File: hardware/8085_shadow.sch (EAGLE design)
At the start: 56 parts, among them IC11 74HCT245DW, IC2 74HCT574N, IC3 74LVC1G04DBV, IC5 74HCT245DW, IC6 74AC273N, IC7 74LVC1G79DBV, IC9 74HCT138N

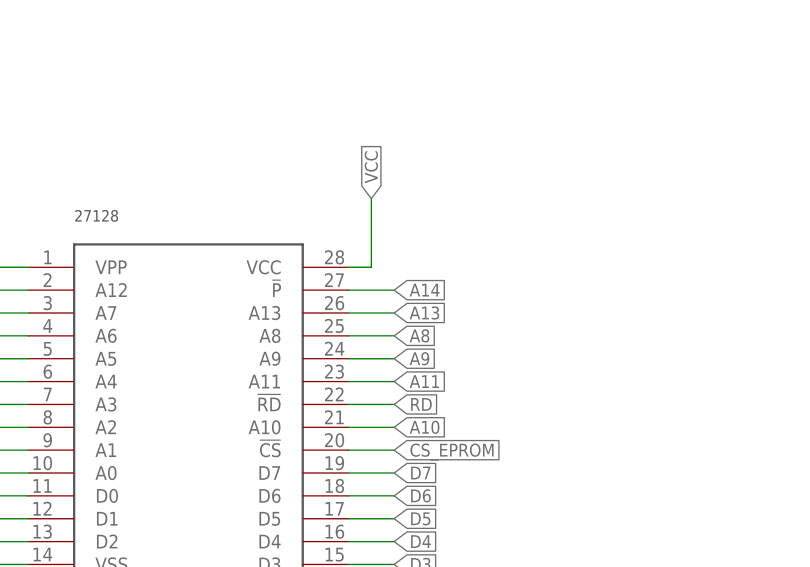
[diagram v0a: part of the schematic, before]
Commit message: Bug in PCB design fixed
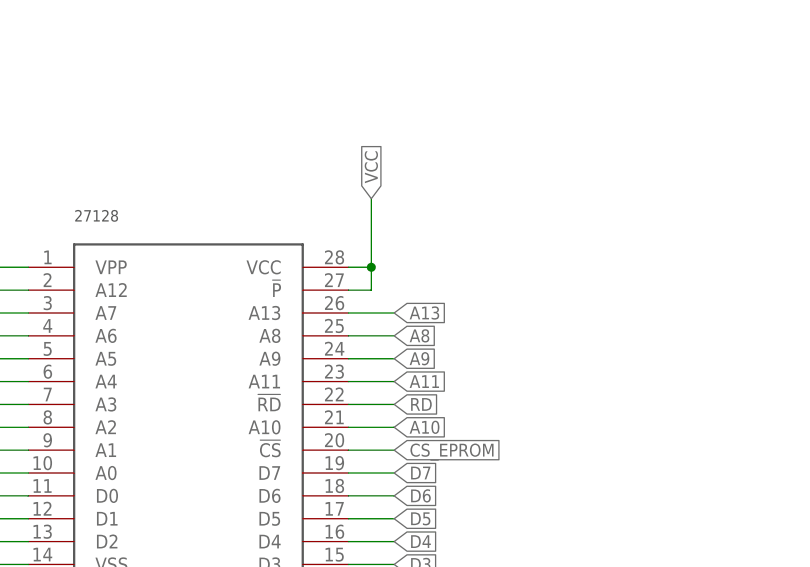
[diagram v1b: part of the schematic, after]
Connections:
- net A14: no longer U$3.!P
- net VCC: now also U$3.!P
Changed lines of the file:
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@@
 <wire x1="284.48" y1="58.42" x2="284.48" y2="66.04" width="0.1524" layer="91"/>
 <label x="284.48" y="66.04" size="1.4224" layer="95" rot="R90" xref="yes"/>
+<pinref part="U$3" gate="G$1" pin="!P"/>
+<wire x1="281.94" y1="55.88" x2="284.48" y2="55.88" width="0.1524" layer="91"/>
+<wire x1="284.48" y1="55.88" x2="284.48" y2="58.42" width="0.1524" layer="91"/>
+<junction x="284.48" y="58.42"/>
 </segment>
 <segment>
@@
 </segment>
 <segment>
-<pinref part="U$3" gate="G$1" pin="!P"/>
-<wire x1="281.94" y1="55.88" x2="287.02" y2="55.88" width="0.1524" layer="91"/>
-<label x="287.02" y="55.88" size="1.4224" layer="95" xref="yes"/>
-</segment>
-<segment>
